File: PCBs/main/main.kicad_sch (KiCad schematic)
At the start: 3 parts, among them J1 Conn_02x02_Odd_Even, J4 Conn_02x10_Odd_Even

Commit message: work on first prototype for the boards
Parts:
- removed A1: Arduino_Mega2560_R3_Shield, PCM_arduino-library:Arduino_Mega2560_R3_Shield, symbol PCM_arduino-library:Arduino_Mega2560_R3_Shield
- removed J1: Conn_02x02_Odd_Even, symbol Connector_Generic:Conn_02x02_Odd_Even
- removed J4: Conn_02x10_Odd_Even, Connector_IDC:IDC-Header_2x10_P2.54mm_Vertical, symbol Connector_Generic:Conn_02x10_Odd_Even
- added A2: Arduino_Mega2560_R3_Shield, PCM_arduino-library:Arduino_Mega2560_R3_Shield, symbol PCM_arduino-library:Arduino_Mega2560_R3_Shield
- added J1, J2, J3, J4: Conn_02x05_Counter_Clockwise, Connector_IDC:IDC-Header_2x05_P2.54mm_Vertical, symbol Connector_Generic:Conn_02x05_Counter_Clockwise
- added J5: chambers 9-10, Connector_IDC:IDC-Header_2x05_P2.54mm_Vertical, symbol Connector_Generic:Conn_02x05_Counter_Clockwise
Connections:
- new net: A2.D26, J3.2 (Pin_2)
- new net: A2.D27, J3.3 (Pin_3)
- new net: A2.D28, J3.4 (Pin_4)
- new net: A2.D29, J3.5 (Pin_5)
- new net: A2.D30, J3.6 (Pin_6)
- new net: A2.D31, J3.7 (Pin_7)
- new net: A2.D32, J3.8 (Pin_8)
- new net: A2.D33, J3.9 (Pin_9)
- new net: A2.D10, J2.2 (Pin_2)
- new net: A2.D11, J2.3 (Pin_3)
- new net: A2.D12, J2.4 (Pin_4)
- new net: A2.D13, J2.5 (Pin_5)
- new net: A2.D22, J2.6 (Pin_6)
- new net: A2.D23, J2.7 (Pin_7)
- new net: A2.D24, J2.8 (Pin_8)
- new net: A2.D25, J2.9 (Pin_9)
- new net: A2.D21 (D21/SCL), J5.2 (Pin_2)
- new net: A2.D20 (D20/SDA), J5.3 (Pin_3)
- new net: A2.D14 (D14/TX3), J5.4 (Pin_4)
- new net: A2.D15 (D15/RX3), J5.5 (Pin_5)
- new net: A2.D16 (D16/TX2), J5.6 (Pin_6)
- new net: A2.D17 (D17/RX2), J5.7 (Pin_7)
- new net: A2.D18 (D18/TX1), J5.8 (Pin_8)
- new net: A2.D19 (D19/RX1), J5.9 (Pin_9)
- new net: A2.D2 (D2_INT0), J1.2 (Pin_2)
- new net: A2.D3 (D3_INT1), J1.3 (Pin_3)
- new net: A2.D34, J4.2 (Pin_2)
- new net: A2.D35, J4.3 (Pin_3)
- new net: A2.D36, J4.4 (Pin_4)
- new net: A2.D37, J4.5 (Pin_5)
- new net: A2.D38, J4.6 (Pin_6)
- new net: A2.D39, J4.7 (Pin_7)
- new net: A2.D4, J1.4 (Pin_4)
- new net: A2.D40, J4.8 (Pin_8)
- new net: A2.D41, J4.9 (Pin_9)
- new net: A2.D5, J1.5 (Pin_5)
- new net: A2.D6, J1.6 (Pin_6)
- new net: A2.D7, J1.7 (Pin_7)
- new net: A2.D8, J1.8 (Pin_8)
- new net: A2.D9, J1.9 (Pin_9)
- new net GND: A2.3V3 (3.3V), A2.GND1 (GND), A2.GND2 (GND), A2.GND3 (GND), A2.GND5 (GND), A2.GND6 (GND), J1.1 (Pin_1), J1.10 (Pin_10), J2.1 (Pin_1), J2.10 (Pin_10), J3.1 (Pin_1), J3.10 (Pin_10), J4.1 (Pin_1), J4.10 (Pin_10), J5.1 (Pin_1), J5.10 (Pin_10)
- no-connect marks 0 -> 37

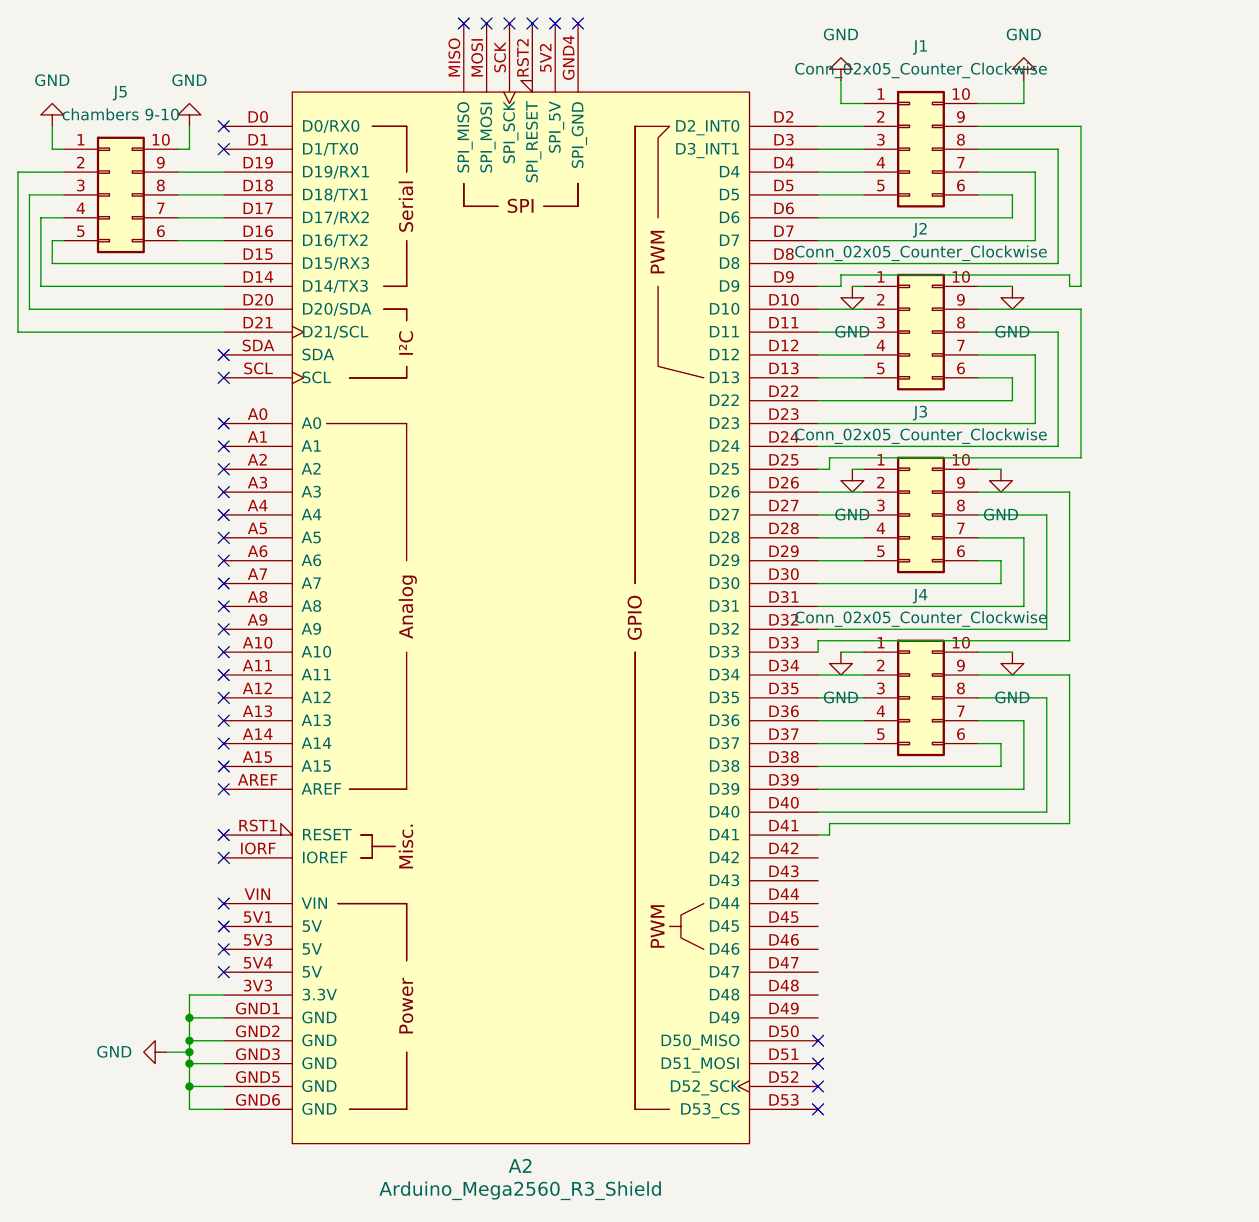
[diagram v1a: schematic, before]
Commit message: update bom and finish first version of PCBs
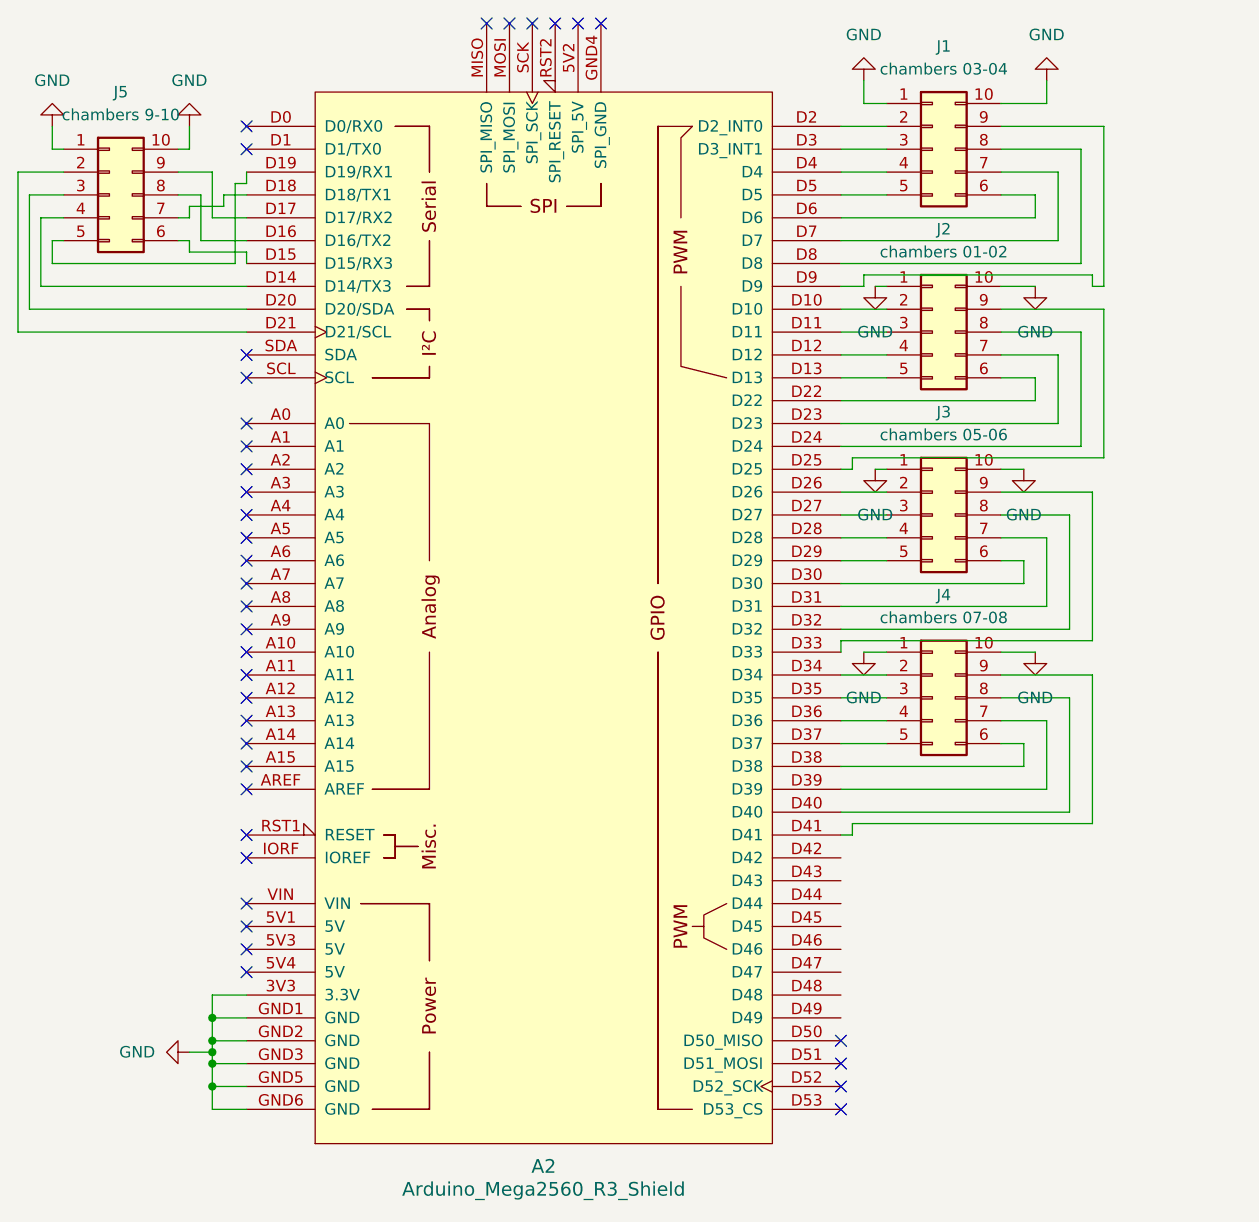
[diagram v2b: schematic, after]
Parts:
- J1: value Conn_02x05_Counter_Clockwise -> chambers 03-04
- J2: value Conn_02x05_Counter_Clockwise -> chambers 01-02
- J3: value Conn_02x05_Counter_Clockwise -> chambers 05-06
- J4: value Conn_02x05_Counter_Clockwise -> chambers 07-08
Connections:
- net at J5.5 (Pin_5): now also A2.D19 (D19/RX1); no longer A2.D15 (D15/RX3)
- net at J5.6 (Pin_6): now also A2.D15 (D15/RX3); no longer A2.D16 (D16/TX2)
- net at J5.7 (Pin_7): now also A2.D18 (D18/TX1); no longer A2.D17 (D17/RX2)
- net at J5.8 (Pin_8): now also A2.D16 (D16/TX2); no longer A2.D18 (D18/TX1)
- net at J5.9 (Pin_9): now also A2.D17 (D17/RX2); no longer A2.D19 (D19/RX1)
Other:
- moved on the sheet: A2, J1, J2, J3, J4
